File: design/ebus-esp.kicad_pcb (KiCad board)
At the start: 2 copper layers, 64.3 x 65.4 mm, 53 parts, among them J1 EBUS, J2 USB_B_Micro, J3 UART, J4 PROG, J5 PINS, J6 PWR, J7 UART, J8 Measurements, Q1 BC817, U1 LM393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

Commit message: Raspberry board update
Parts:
- removed C1: 330nF, Capacitor_SMD:C_1206_3216Metric
- removed C6: 100nF, Capacitor_SMD:C_1206_3216Metric
- removed D1: 1N4737A 7.5V, Diode_SMD:D_SOD-123
- removed D2: TX red, LED_THT:LED_D3.0mm_Horizontal_O1.27mm_Z2.0mm
- removed D3: DF10M, Diode_SMD:Diode_Bridge_Bourns_CD-DF4xxS
- removed D4: RX green, LED_THT:LED_D3.0mm_Horizontal_O1.27mm_Z2.0mm
- removed D5: EBUS yellow, LED_THT:LED_D3.0mm_Horizontal_O1.27mm_Z2.0mm
- removed D6: ESP blue, LED_THT:LED_D3.0mm_Horizontal_O1.27mm_Z2.0mm
- removed D7: 1N914, Package_TO_SOT_SMD:SOT-23
- removed H1, H2, H3, H4: MountingHole, MountingHole:MountingHole_3.2mm_M3
- removed J1: EBUS, TerminalBlock_4Ucon:TerminalBlock_4Ucon_1x02_P3.50mm_Horizontal
- removed J3: UART, Connector_PinSocket_2.54mm:PinSocket_2x05_P2.54mm_Vertical
- removed J8: Measurements, Connector_PinHeader_1.27mm:PinHeader_2x07_P1.27mm_Vertical
- removed Q1: BC817, Package_TO_SOT_SMD:SOT-23
- removed R1, R16: 220, Resistor_SMD:R_1206_3216Metric
- removed R10: 220k, Resistor_SMD:R_1206_3216Metric
- removed R11, R17, R19: 10k, Resistor_SMD:R_1206_3216Metric
- removed R13, R6: 470, Resistor_SMD:R_1206_3216Metric
- removed R14: 390, Resistor_SMD:R_1206_3216Metric
- removed R15: 820, Resistor_SMD:R_1206_3216Metric
- removed R3: 100k, Resistor_SMD:R_1206_3216Metric
- removed R4: 22k, Resistor_SMD:R_1206_3216Metric
- removed R7: 15k, Resistor_SMD:R_1206_3216Metric
- removed R9: 18k, Resistor_SMD:R_1206_3216Metric
- removed U1: LM393, Package_SO:SOIC-8_3.9x4.9mm_P1.27mm
- removed U2, U4: LTV-357T, Package_SO:SO-4_4.4x3.6mm_P2.54mm
- removed U3: L7805, Package_TO_SOT_SMD:TO-263-2
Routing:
- removed copper zone on B.Cu, net (none)
- removed copper zone on F.Cu, net GNDD
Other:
- board size 64.3 x 65.4 mm -> 30.1 x 65.3 mm
- board text removed: "1"
- board text removed: "10"
- board text removed: "11"
- board text removed: "12"
- board text removed: "13"
- board text removed: "3"
- board text removed: "4"
- board text removed: "5"
- board text removed: "6"
- board text removed: "7"
- board text removed: "9"
- board text removed: "COM"
- board text removed: "EBUS"
- board text removed: "blue"
- board text removed: "green"
- board text removed: "red"
- board text removed: "smart home"
- board text removed: "yellow"

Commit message: Gerbers
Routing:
- net GNDD: track 162.4 -> 0.00 mm, vias 7 -> 0
- net MP5: track 106.7 -> 0.00 mm, vias 4 -> 0
- net MP1: track 75.9 -> 0.00 mm, vias 2 -> 0
- net MP12: track 75.4 -> 0.00 mm, vias 3 -> 0
- net MP4: track 68.2 -> 0.00 mm, vias 3 -> 0
- net MP11: track 67.1 -> 0.00 mm, vias 3 -> 0
- net GNDREF: track 218.0 -> 153.9 mm, vias 3 -> 2
- net +3V3: track 173.7 -> 111.1 mm, vias 4 -> 3
- net SIGNAL: track 60.5 -> 0.00 mm, vias 2 -> 0
- net RX: track 112.8 -> 52.8 mm, vias 4 -> 3
- net MP9: track 59.0 -> 0.00 mm, vias 5 -> 0
- net MP6: track 51.6 -> 0.00 mm, vias 4 -> 0
- net MP10: track 51.2 -> 0.00 mm, vias 3 -> 0
- net MP13: track 50.2 -> 0.00 mm, vias 4 -> 0
- net MP3: track 48.5 -> 0.00 mm, vias 2 -> 0
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
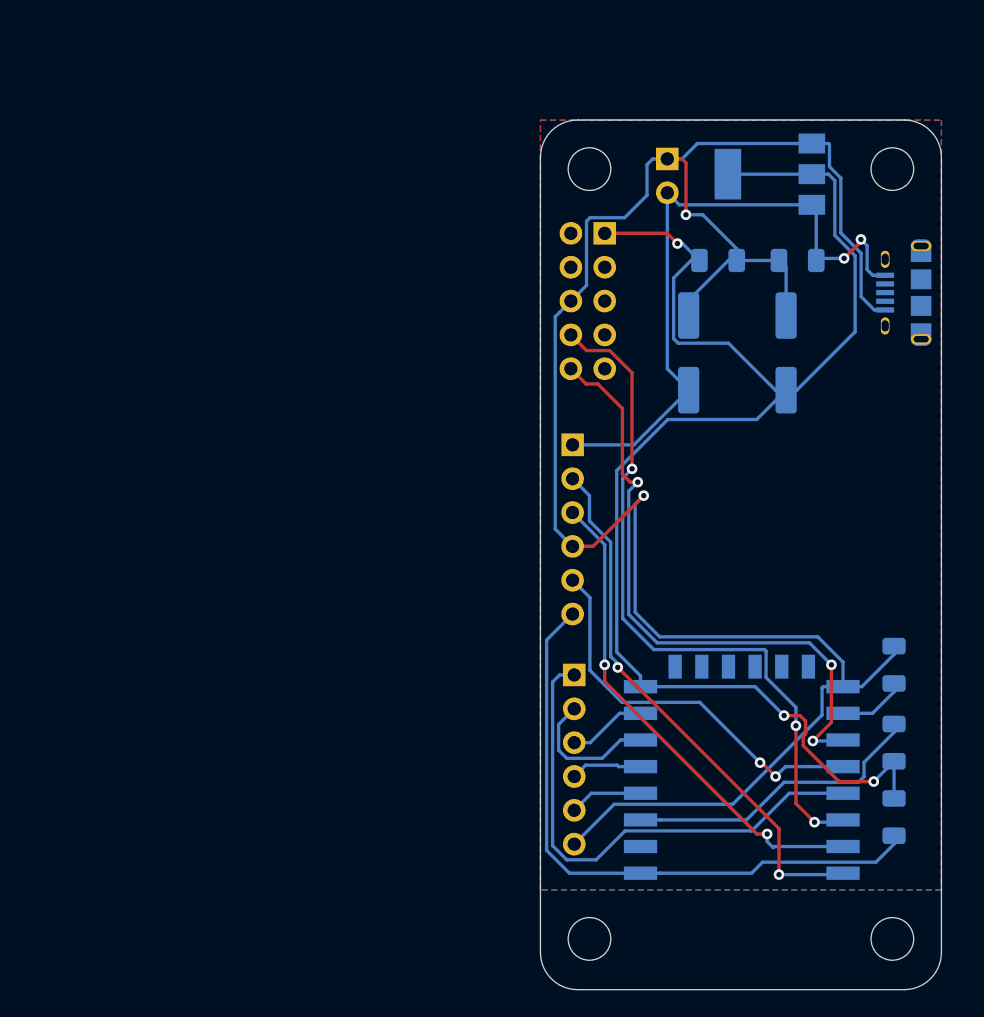
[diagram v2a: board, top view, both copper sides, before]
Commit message: Inverted rx-tx, reposition ebus terminal with measurement points to let attach raspberry with full connector, added programmer to wifi module
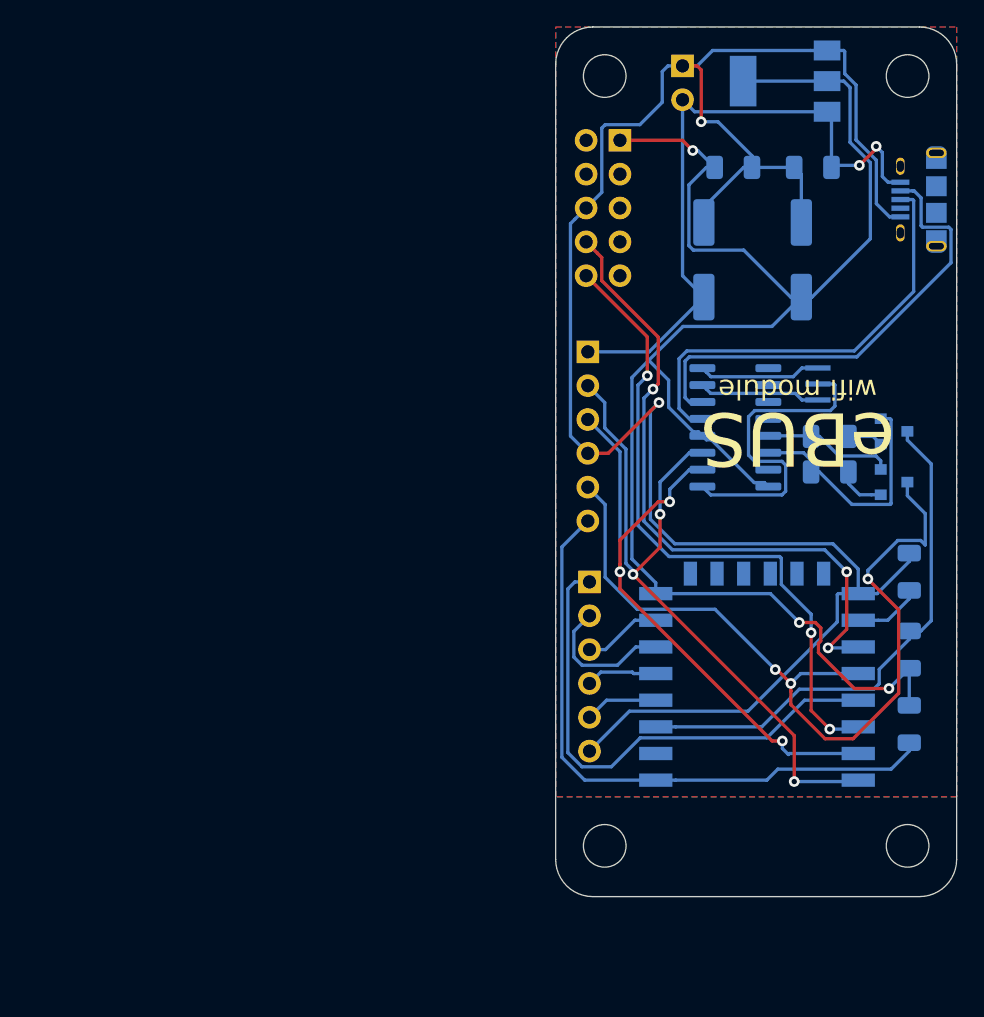
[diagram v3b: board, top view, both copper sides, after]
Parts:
- added Q2: BC817, Package_TO_SOT_SMD:SOT-23, B.Cu at (124.0, 106.6)
- added Q3: BC817, Package_TO_SOT_SMD:SOT-23, B.Cu at (124.0, 110.4)
- added R2: 10k, Resistor_SMD:R_1206_3216Metric, B.Cu at (119.1, 106.9)
- added R5: 10k, Resistor_SMD:R_1206_3216Metric, B.Cu at (119.1, 109.6)
- added U7: CH340G, Package_SO:SOIC-16_3.9x9.9mm_P1.27mm, B.Cu at (112.0, 106.3)
- added Y1: 12MHz 22pF, Crystal:Resonator_SMD_muRata_CSTxExxV-3Pin_3.0x1.1mm, B.Cu at (118.2, 103.0)
- moved U6 7.08 mm to (113.7, 129.2)
- moved C2 7.08 mm to (117.9, 86.7)
- moved C3 7.08 mm to (109.7, 93.7)
- moved C4 7.08 mm to (111.9, 86.7)
- moved C5 7.08 mm to (117.0, 93.7)
- moved H5 7.08 mm to (125.0, 79.9)
- moved H7 7.08 mm to (102.2, 79.9)
- moved J2 7.08 mm to (127.1, 89.2)
- moved J4 7.08 mm to (101.0, 100.6)
- moved J5 7.08 mm to (101.1, 117.9)
- moved J6 7.08 mm to (108.1, 79.1)
- moved J7 7.08 mm to (103.4, 84.7)
- moved R21 7.08 mm to (125.1, 117.1)
- moved U5 7.08 mm to (115.8, 80.3)
- moved H6 7.08 mm to (125.0, 137.7)
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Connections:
- C2 pad 1: +5VP -> (no net)
- C2 pad 2: GNDREF -> (no net)
- C3 pad 1: +5VP -> (no net)
- C3 pad 2: GNDREF -> (no net)
- C4 pad 1: +3V3 -> (no net)
- C4 pad 2: GNDREF -> (no net)
- C5 pad 1: +3V3 -> (no net)
- C5 pad 2: GNDREF -> (no net)
- J2 pad 1: +5VP -> (no net)
- J2 pad 5: GNDREF -> (no net)
- J4 pad 1: +5VP -> (no net)
- J4 pad 2: P_TX -> (no net)
- J4 pad 3: P_RX -> (no net)
- J4 pad 4: GNDREF -> (no net)
- J4 pad 5: GPIO0 -> (no net)
- J4 pad 6: RESET -> (no net)
- J5 pad 1: GPIO4 -> (no net)
- J5 pad 2: GPIO12 -> (no net)
- J5 pad 3: GPIO13 -> (no net)
- J5 pad 4: GPIO14 -> (no net)
- J5 pad 5: GPIO16 -> (no net)
- J5 pad 6: GNDREF -> (no net)
- J6 pad 1: GNDREF -> (no net)
- J6 pad 2: +5VP -> (no net)
- J7 pad 1: +3V3 -> (no net)
- J7 pad 10: TX -> (no net)
- J7 pad 6: GNDREF -> (no net)
- J7 pad 8: RX -> (no net)
- R18 pad 1: Net-(R18-Pad1) -> (no net)
- R18 pad 2: +3V3 -> (no net)
- R20 pad 1: RESET -> (no net)
- R20 pad 2: +3V3 -> (no net)
- R21 pad 1: GNDREF -> (no net)
- R21 pad 2: Net-(R21-Pad2) -> (no net)
- U5 pad 1: GNDREF -> (no net)
- U5 pad 2: +3V3 -> (no net)
- U5 pad 3: +5VP -> (no net)
- U6 pad 1: RESET -> (no net)
- U6 pad 15: GNDREF -> (no net)
- U6 pad 16: Net-(R21-Pad2) -> (no net)
- U6 pad 17: TX -> (no net)
- U6 pad 18: GPIO0 -> (no net)
- U6 pad 19: GPIO4 -> (no net)
- U6 pad 20: RX -> (no net)
- U6 pad 21: P_RX -> (no net)
- U6 pad 22: P_TX -> (no net)
- U6 pad 3: Net-(R18-Pad1) -> (no net)
- U6 pad 4: GPIO16 -> (no net)
- U6 pad 5: GPIO14 -> (no net)
- U6 pad 6: GPIO12 -> (no net)
- U6 pad 7: GPIO13 -> (no net)
- U6 pad 8: +3V3 -> (no net)
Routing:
- net (no net): track 0.00 -> 895.4 mm, vias 0 -> 22
- net GNDREF: track 153.9 -> 0.00 mm, vias 2 -> 0
- net +3V3: track 111.1 -> 0.00 mm, vias 3 -> 0
- net RX: track 52.8 -> 0.00 mm, vias 3 -> 0
- net +5VP: track 49.5 -> 0.00 mm, vias 2 -> 0
- net TX: track 47.0 -> 0.00 mm, vias 3 -> 0
- net RESET: track 46.9 -> 0.00 mm
- net P_TX: track 41.0 -> 0.00 mm, vias 2 -> 0
- net GPIO4: track 38.4 -> 0.00 mm
- net P_RX: track 37.1 -> 0.00 mm, vias 2 -> 0
- net GPIO0: track 29.9 -> 0.00 mm, vias 2 -> 0
- net Net-(R18-Pad1): track 23.0 -> 0.00 mm
- net GPIO12: track 10.6 -> 0.00 mm
- net GPIO13: track 5.88 -> 0.00 mm
- net GPIO16: track 5.50 -> 0.00 mm
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- added copper zone on B.Cu, net (none)
- added copper zone on F.Cu, net (none)
- removed copper zone on B.Cu, net GNDREF
- removed copper zone on F.Cu, net GNDREF

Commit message: usbc, updated images
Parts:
- added C7: 22pF, Capacitor_SMD:C_0805_2012Metric, B.Cu at (94.3, 115.5)
- added C8: 22pF, Capacitor_SMD:C_0805_2012Metric, B.Cu at (98.7, 115.5)
- J2: value USB_B_Micro -> USB_C_Receptacle_USB2.0; footprint usb:AMPHENOL_10118194-0001LF -> Connector_USB:USB_C_Receptacle_HRO_TYPE-C-31-M-12
- Y1: value 12MHz 22pF -> Crystal; footprint Crystal:Resonator_SMD_muRata_CSTxExxV-3Pin_3.0x1.1mm -> Crystal:Crystal_SMD_HC49-SD
- moved J2 26.6 mm to (101.9, 80.8), turned to 0 degrees
- moved U5 18.5 mm to (108.9, 97.5), turned to -90 degrees
- moved Y1 16.6 mm to (103.3, 110.1)
- moved Q2 16.0 mm to (108.1, 105.1)
- moved Q3 16.0 mm to (108.1, 108.9)
- moved C3 15.8 mm to (94.1, 95.8)
- moved C4 15.8 mm to (96.3, 88.9)
- moved C5 15.8 mm to (101.4, 95.8)
- moved H5 15.8 mm to (109.4, 82.0)
- moved H6 15.8 mm to (109.4, 139.8)
- moved H7 15.8 mm to (86.6, 82.0)
- moved H8 15.8 mm to (86.6, 139.8)
- moved J4 15.8 mm to (85.4, 102.7)
- moved J5 15.8 mm to (85.5, 120.0)
- moved J7 15.8 mm to (87.8, 86.9)
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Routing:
- net (no net): track 895.4 -> 977.9 mm, vias 22 -> 33
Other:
- net class Default removed
- net class Power removed
- board text removed: "eBUS"
- board text removed: "wifi module"
- board text removed: "~"
